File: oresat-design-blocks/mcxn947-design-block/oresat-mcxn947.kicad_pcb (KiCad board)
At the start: 4 copper layers, 153 x 110 mm, 68 parts, among them J1 BKUP-BATT, J2 USB_C_Receptacle_USB2.0_14P, J3 CAN, J4 TERM, J5 10pin ARM SWD, J6 FTDI-UART-6PIN, SW1 RESET, SW2 ISP(BOOT), U1 MCXN947VKLT, U2 TCAN330, Y1 24 MHz, Y2 32.768 KHz

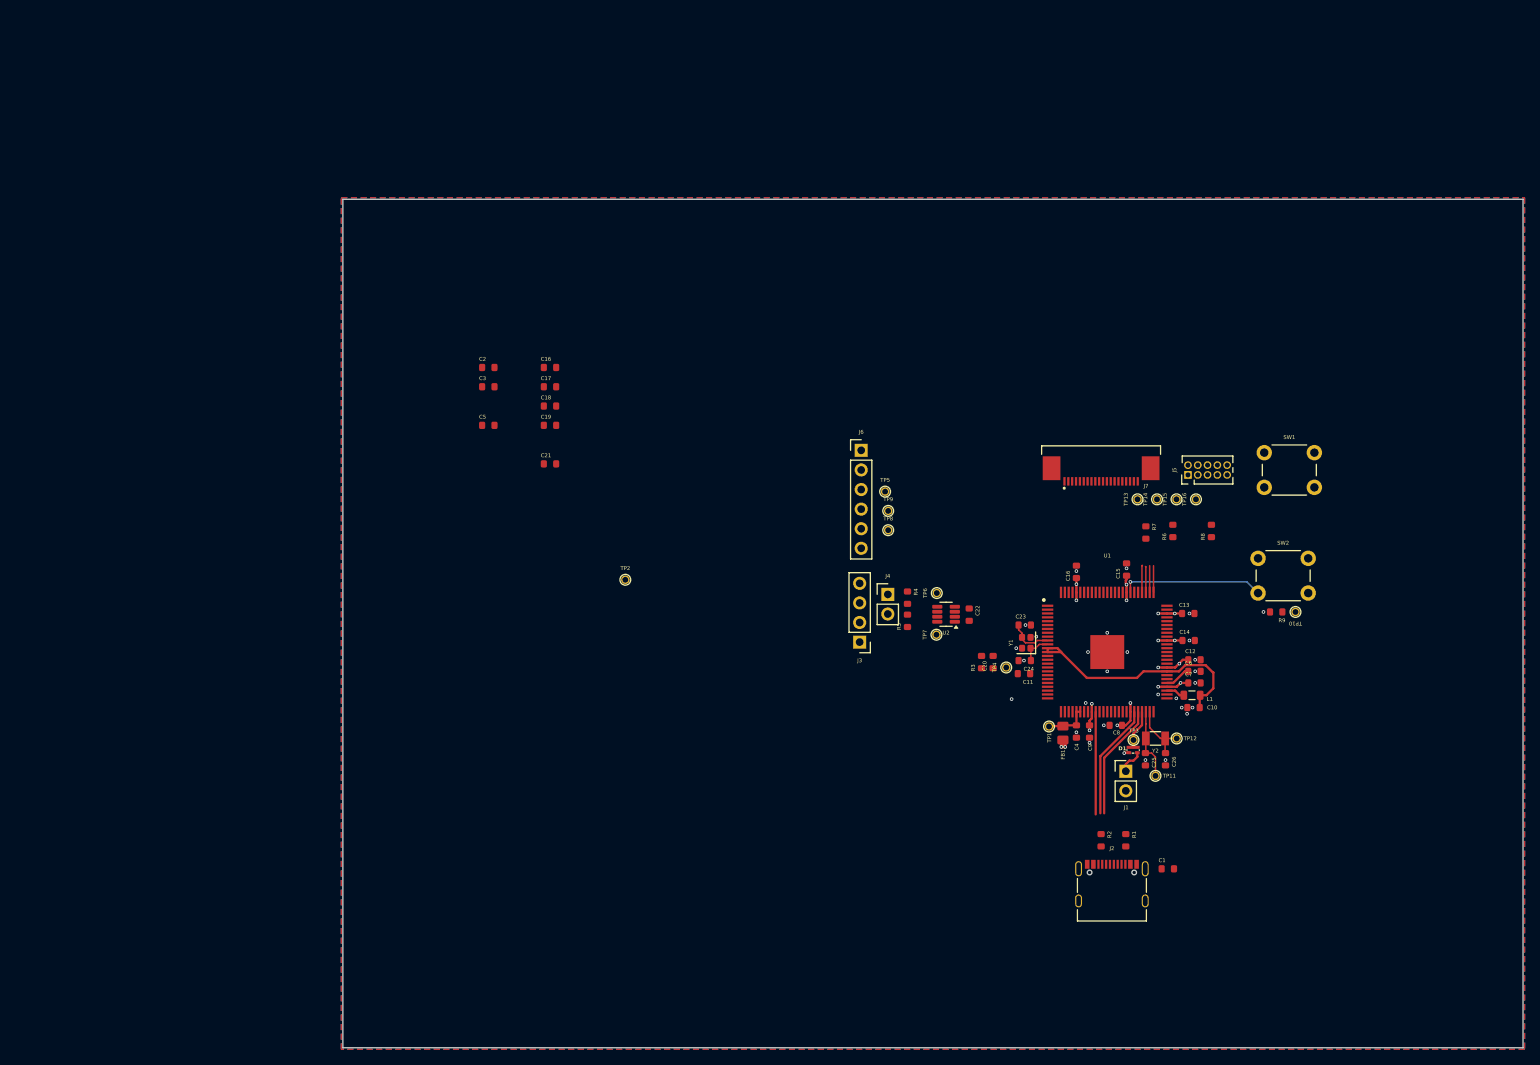
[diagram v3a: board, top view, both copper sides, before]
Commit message: Added 3.3V SPS but not hooked up yet. Everything else a rough draft, except for pin breakouts.
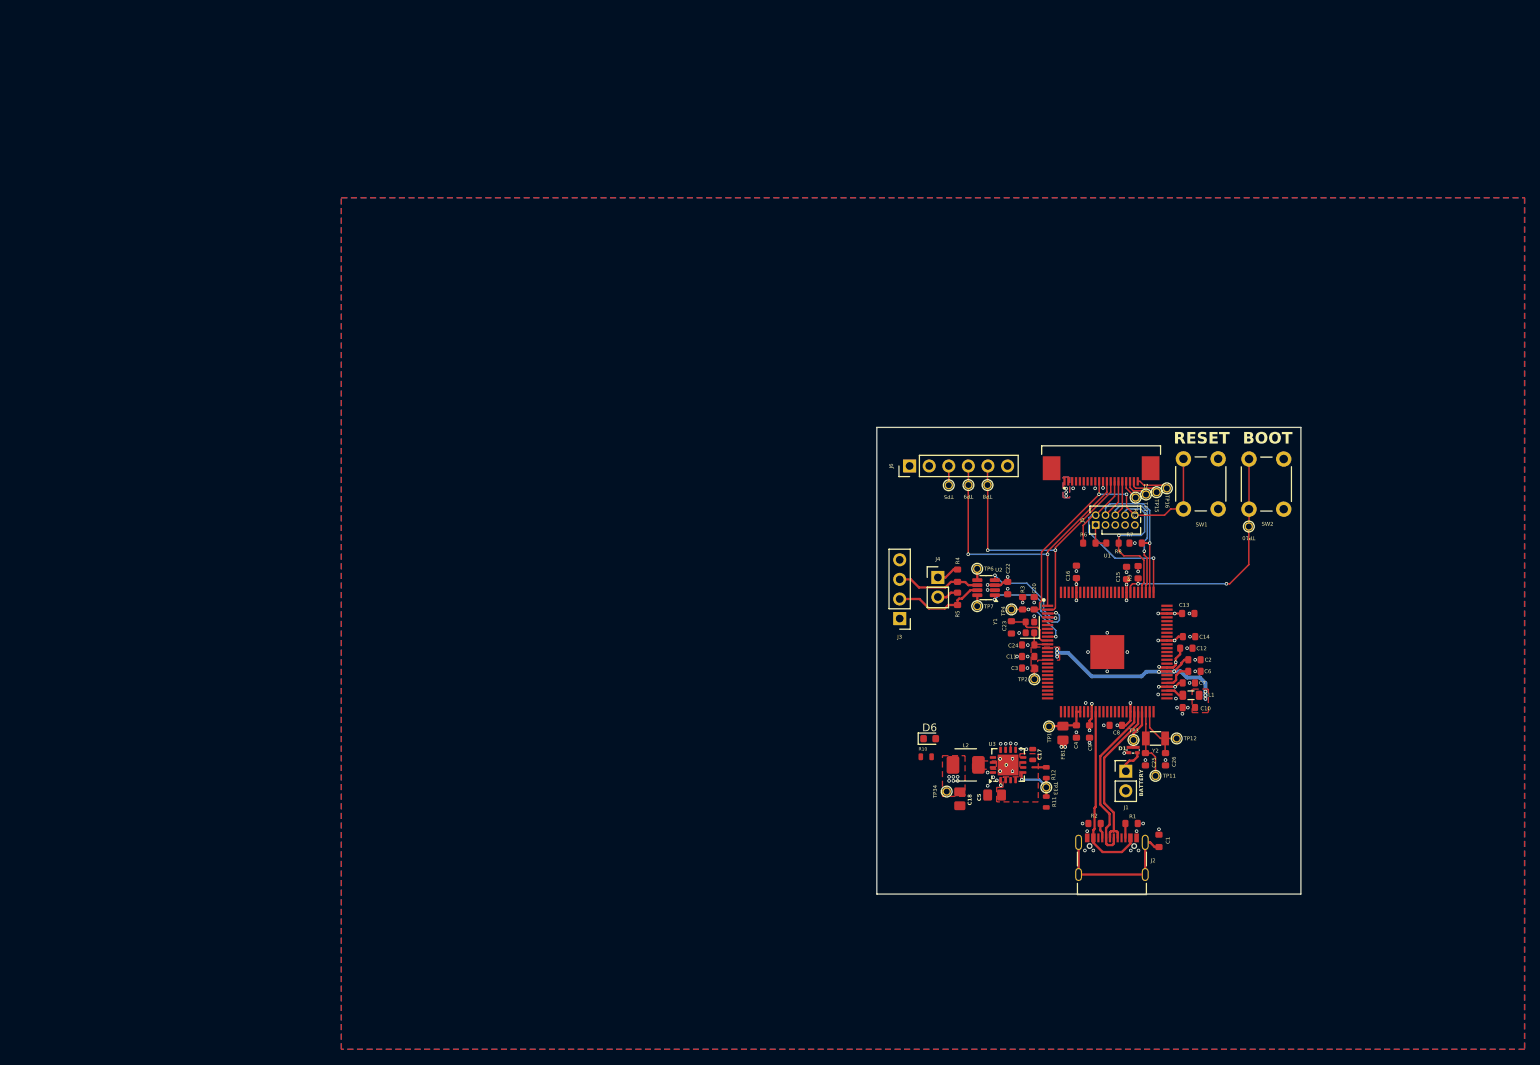
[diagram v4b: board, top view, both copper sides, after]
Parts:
- removed the C16 at (88.3, 63.8)
- removed C19, C21: 100n, oresat-passives:0603-B-NOSILK
- added D6: GREEN, LED_SMD:LED_0603_1608Metric, F.Cu at (137.5, 111.9)
- added L2: 6.8u, oresat-passives:L_ECS-MPI4040, F.Cu at (142.1, 115.3)
- added R10: 10k, oresat-passives:0603-C-NOSILK, F.Cu at (137.0, 114.3)
- added R11: 10k, oresat-passives:0603-C-NOSILK, F.Cu at (152.6, 120.1)
- added R12: 10k, oresat-passives:0603-C-NOSILK, F.Cu at (152.6, 116.3)
- added TP33: Test-Point, oresat-misc:TestPoint-0.75mm-th, F.Cu at (152.6, 118.2)
- added TP34: Test-Point, oresat-misc:TestPoint-0.75mm-th, F.Cu at (139.7, 118.8)
- added U3: TPS62111RSA, Package_DFN_QFN:Texas_RSA_VQFN-16-1EP_4x4mm_P0.65mm_EP2.7x2.7mm, F.Cu at (147.6, 115.3)
- C17: value 100n -> 1u; footprint oresat-passives:0603-B-NOSILK -> oresat-passives:0603-C-NOSILK
- C18: value 100n -> 22u; footprint oresat-passives:0603-B-NOSILK -> oresat-passives:0805-B-NOSILK
- C5: value 100n -> 10u; footprint oresat-passives:0603-B-NOSILK -> oresat-passives:0805-B-NOSILK
- moved C2 99.1 mm to (171.8, 101.7)
- moved C5 81.3 mm to (145.9, 119.2), turned to 180 degrees
- moved C3 78.9 mm to (150.2, 102.8), turned to 180 degrees
- moved C17 78.7 mm to (150.8, 114.0), turned to 90 degrees
- moved C18 73.6 mm to (141.4, 119.7), turned to -90 degrees
- moved TP2 54.6 mm to (151.1, 104.2)
- moved R9 18.6 mm to (164.5, 90.3), turned to 90 degrees
- moved TP8 14.1 mm to (145.0, 79.0), turned to 180 degrees
- moved J5 13.6 mm to (159.0, 84.2)
- moved SW2 13.3 mm to (183.4, 75.7), turned to -90 degrees
- moved R8 12.9 mm to (161.2, 86.6), turned to 180 degrees
- moved SW1 12.8 mm to (170.4, 82.2), turned to 90 degrees
- moved TP10 12.6 mm to (178.8, 84.4)
- moved R6 10.9 mm to (158.2, 86.6), turned to 0 degrees
- moved TP9 10.9 mm to (142.5, 79.0), turned to 180 degrees
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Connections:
- C17 pad 1: +3.3V -> VBUS
- C5 pad 1: VDD -> VBUS
- J3 pad 1: +3.3V -> VBUS
- J7 pad 1: +3.3V -> VBUS
- J7 pad 2: +3.3V -> VBUS
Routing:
- net VBUS: track 13.3 -> 101.2 mm, vias 0 -> 3
- net RESET: track 0.00 -> 49.8 mm, vias 0 -> 4
- net /ISP-UART_RXD: track 0.00 -> 41.1 mm, vias 0 -> 2
- net /ISP-UART_TXD: track 0.00 -> 40.2 mm, vias 0 -> 2
- net /SWDIO: track 3.46 -> 27.0 mm, vias 0 -> 1
- net /SWCLK: track 3.46 -> 24.6 mm, vias 0 -> 1
- net Net-(J2-SHIELD): track 0.00 -> 19.0 mm
- net /SWO: track 3.38 -> 20.9 mm, vias 0 -> 1
- net /SWI: track 3.53 -> 19.4 mm, vias 0 -> 1
- net /CAN_TXD: track 0.00 -> 13.8 mm, vias 0 -> 2
- net /BOOT: track 18.5 -> 31.7 mm, vias 1 -> 2
- net /CAN_RXD: track 0.00 -> 12.6 mm, vias 0 -> 2
- net /CANH: track 0.00 -> 11.9 mm
- net /CANL: track 0.00 -> 11.0 mm
- net +3.3V: track 32.8 -> 42.5 mm, vias 20 -> 31
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- added copper zone on F.Cu, net +3.3V
- added copper zone on In2.Cu, net GND
- added copper zone on F.Cu, net Net-(L2-Pad1)
- added copper zone on B.Cu, net VBUS
- added copper zone on F.Cu, net VBUS
- added copper zone on In2.Cu, net VBUS
- added copper zone on F.Cu, net VDD
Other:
- board size 153 x 110 mm -> 55 x 60.5 mm
- board text added: "BATTERY"
- board text added: "BOOT"
- board text added: "RESET"

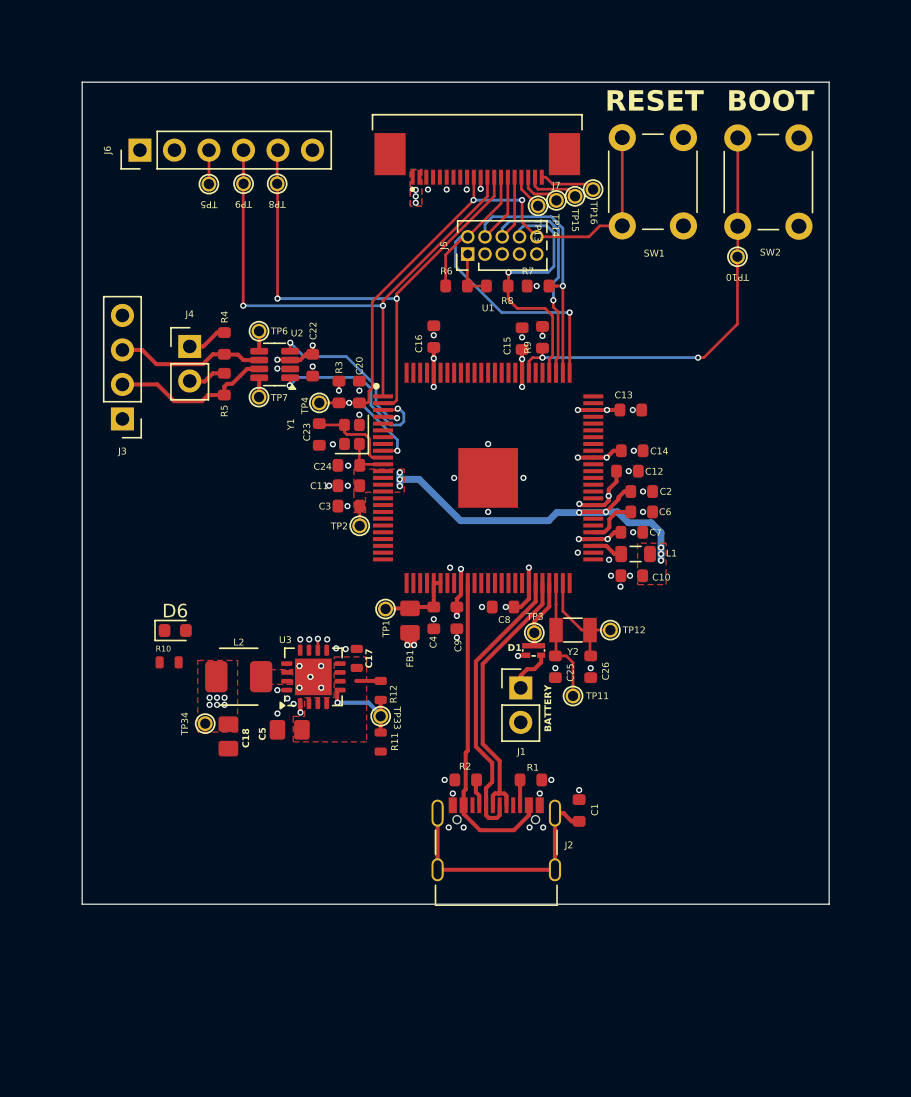
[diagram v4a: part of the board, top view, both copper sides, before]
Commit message: added hierarchal sheets, cleaned up schematic, added and routed breakout connectors
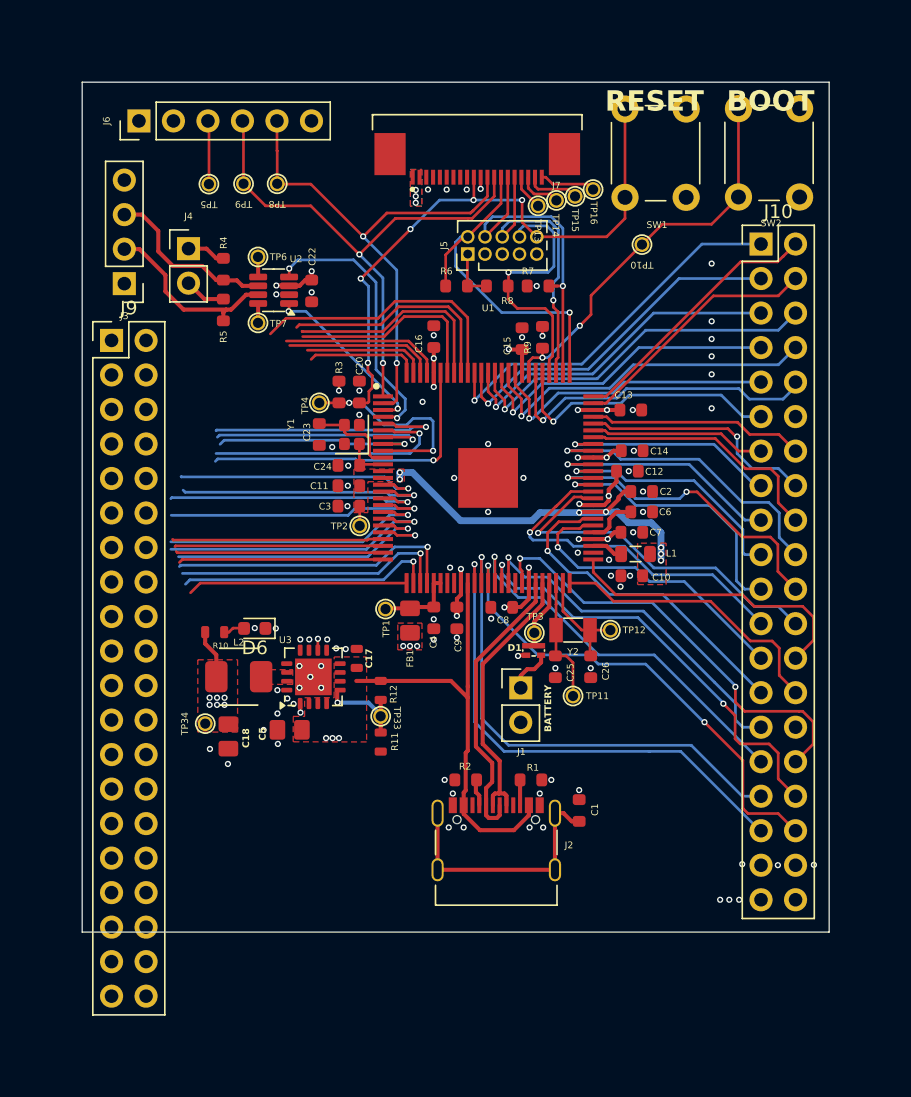
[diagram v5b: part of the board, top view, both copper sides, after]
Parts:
- added J10: Conn_02x20_Odd_Even, Connector_PinHeader_2.54mm:PinHeader_2x20_P2.54mm_Vertical, F.Cu at (180.6, 83.5)
- added J9: Conn_02x20_Odd_Even, Connector_PinHeader_2.54mm:PinHeader_2x20_P2.54mm_Vertical, F.Cu at (132.8, 90.6)
- moved J3 9.96 mm to (133.7, 86.4)
- moved J4 7.20 mm to (138.4, 83.8)
- moved TP10 7.08 mm to (171.8, 83.5)
- moved D6 5.86 mm to (143.3, 111.8), turned to 180 degrees
- moved C22 5.46 mm to (147.5, 86.9)
- moved TP6 5.46 mm to (143.6, 84.4)
- moved TP7 5.46 mm to (143.6, 89.3)
- moved R4 5.46 mm to (141.0, 85.3)
- moved R5 5.46 mm to (141.0, 88.3)
- moved U2 5.46 mm to (144.7, 86.9)
- moved R10 4.02 mm to (140.4, 112.0), turned to 180 degrees
- moved J6 2.15 mm to (134.8, 74.4)
- moved SW2 2.15 mm to (183.4, 73.5)
- moved SW1 2.11 mm to (170.6, 80.0)
- moved C8 0.10 mm to (161.5, 110.2)
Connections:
- net /BOOT renamed /Power & Signal/BOOT
- net /CANH renamed /Power & Signal/CANH
- net /CANL renamed /Power & Signal/CANL
- net /CAN_RXD renamed Net-(U1C-P1_11)
- net /CAN_TXD renamed Net-(U1C-P1_10)
- net /SWI renamed Net-(J5-NC/TDI)
- J5 pad 2: /SWDIO -> Net-(J5-SWDIO/TMS)
- J5 pad 4: /SWCLK -> Net-(J5-SWCLK/TCK)
- J5 pad 6: /SWO -> Net-(J5-SWO/TDO)
- J6 pad 4: /ISP-UART_RXD -> Net-(J6-TXD)
- J6 pad 5: /ISP-UART_TXD -> Net-(J6-RXD)
- J7 pad 12: /ISP-UART_RXD -> ISP-UART_RXD
- J7 pad 13: /ISP-UART_TXD -> ISP-UART_TXD
- J7 pad 14: /SWDIO -> SWDIO
- J7 pad 15: /SWCLK -> SWCLK
- J7 pad 16: /SWO -> SWO
- R6 pad 1: /SWDIO -> Net-(J5-SWDIO/TMS)
- R7 pad 2: /SWCLK -> Net-(J5-SWCLK/TCK)
- TP8 pad 1: /ISP-UART_TXD -> Net-(J6-RXD)
- TP9 pad 1: /ISP-UART_RXD -> Net-(J6-TXD)
- U1 pad 1: /ISP-UART_RXD -> Net-(J6-TXD)
- U1 pad 100: unconnected-(U1C-P1_7-Pad100) -> P1_7
- U1 pad 2: /ISP-UART_TXD -> Net-(J6-RXD)
- U1 pad 36: unconnected-(U1F-P4_13/ANA_14-Pad36) -> P4_13
- U1 pad 37: unconnected-(U1F-P4_15-Pad37) -> P4_15
- U1 pad 38: unconnected-(U1F-P4_16-Pad38) -> P4_16
- U1 pad 39: unconnected-(U1F-P4_17/ANA_18-Pad39) -> P4_17
- U1 pad 40: unconnected-(U1F-P4_19-Pad40) -> P4_19
- U1 pad 41: unconnected-(U1F-P4_20-Pad41) -> P4_20
- U1 pad 43: unconnected-(U1F-P4_23-Pad43) -> P4_23
- U1 pad 5: unconnected-(U1C-P1_12-Pad5) -> P1_12
- U1 pad 50: unconnected-(U1G-P5_2-Pad50) -> P5_2
- U1 pad 51: unconnected-(U1G-P5_3-Pad51) -> P5_3
- U1 pad 56: unconnected-(U1E-P3_21-Pad56) -> Net-(J10-Pin_25)
- U1 pad 57: unconnected-(U1E-P3_20-Pad57) -> Net-(J10-Pin_27)
- U1 pad 6: unconnected-(U1C-P1_13-Pad6) -> P1_13
- U1 pad 60: unconnected-(U1E-P3_17-Pad60) -> Net-(J10-Pin_24)
- U1 pad 61: unconnected-(U1E-P3_16-Pad61) -> Net-(J10-Pin_23)
- U1 pad 62: unconnected-(U1E-P3_15-Pad62) -> Net-(J10-Pin_21)
- U1 pad 63: unconnected-(U1E-P3_14-Pad63) -> Net-(J10-Pin_22)
- U1 pad 64: unconnected-(U1E-P3_13-Pad64) -> Net-(J10-Pin_19)
- U1 pad 65: unconnected-(U1E-P3_12-Pad65) -> Net-(J10-Pin_17)
- U1 pad 67: unconnected-(U1E-P3_11-Pad67) -> Net-(J10-Pin_20)
- U1 pad 68: unconnected-(U1E-P3_10-Pad68) -> Net-(J10-Pin_15)
- U1 pad 69: unconnected-(U1E-P3_9-Pad69) -> Net-(J10-Pin_18)
- U1 pad 7: unconnected-(U1C-P1_14-Pad7) -> P1_14
- U1 pad 70: unconnected-(U1E-P3_8-Pad70) -> Net-(J10-Pin_13)
- U1 pad 71: unconnected-(U1E-P3_7-Pad71) -> Net-(J10-Pin_16)
- U1 pad 72: unconnected-(U1E-P3_6-Pad72) -> Net-(J10-Pin_14)
- U1 pad 74: unconnected-(U1E-P3_1-Pad74) -> Net-(J10-Pin_4)
- U1 pad 75: unconnected-(U1E-P3_0-Pad75) -> Net-(J10-Pin_2)
- U1 pad 76: /SWDIO -> Net-(J5-SWDIO/TMS)
- U1 pad 77: /SWCLK -> Net-(J5-SWCLK/TCK)
- U1 pad 78: /SWO -> Net-(J5-SWO/TDO)
- U1 pad 8: unconnected-(U1C-P1_15-Pad8) -> P1_15
- U1 pad 80: unconnected-(U1B-P0_4-Pad80) -> P0_4
- U1 pad 81: unconnected-(U1B-P0_5-Pad81) -> P0_5
- U1 pad 84: unconnected-(U1B-P0_16-Pad84) -> P0_16
- U1 pad 85: unconnected-(U1B-P0_17-Pad85) -> P0_17
- U1 pad 86: unconnected-(U1B-P0_18-Pad86) -> P0_18
- U1 pad 87: unconnected-(U1B-P0_19-Pad87) -> P0_19
- U1 pad 88: unconnected-(U1B-P0_20-Pad88) -> P0_20
- U1 pad 89: unconnected-(U1B-P0_21-Pad89) -> P0_21
- U1 pad 90: unconnected-(U1B-P0_22-Pad90) -> P0_22
- U1 pad 91: unconnected-(U1B-P0_23-Pad91) -> P0_23
- U1 pad 92: unconnected-(U1C-P1_0-Pad92) -> P1_0
- U1 pad 93: unconnected-(U1C-P1_1-Pad93) -> P1_1
- U1 pad 94: unconnected-(U1C-P1_2-Pad94) -> P1_2
- U1 pad 95: unconnected-(U1C-P1_3-Pad95) -> P1_3
- U1 pad 97: unconnected-(U1C-P1_4-Pad97) -> P1_4
- U1 pad 98: unconnected-(U1C-P1_5-Pad98) -> P1_5
- U1 pad 99: unconnected-(U1C-P1_6-Pad99) -> P1_6
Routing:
- net /ISP-UART_RXD: track 41.1 -> 0.00 mm, vias 2 -> 0
- net /ISP-UART_TXD: track 40.2 -> 0.00 mm, vias 2 -> 0
- net P4_13: track 0.00 -> 37.6 mm, vias 0 -> 1
- net P4_15: track 0.00 -> 36.7 mm, vias 0 -> 1
- net P4_16: track 0.00 -> 35.8 mm, vias 0 -> 2
- net Net-(J6-RXD): track 0.00 -> 35.6 mm, vias 0 -> 2
- net P4_23: track 0.00 -> 32.6 mm, vias 0 -> 2
- net P4_19: track 0.00 -> 32.5 mm, vias 0 -> 2
- net P4_17: track 0.00 -> 28.7 mm, vias 0 -> 1
- net P0_22: track 0.00 -> 27.9 mm, vias 0 -> 1
- net P0_19: track 0.00 -> 27.3 mm, vias 0 -> 1
- net Net-(J10-Pin_24): track 0.00 -> 27.0 mm, vias 0 -> 1
- net SWDIO: track 0.00 -> 27.0 mm, vias 0 -> 1
- net /SWDIO: track 27.0 -> 0.00 mm, vias 1 -> 0
- net P4_20: track 0.00 -> 26.5 mm, vias 0 -> 1
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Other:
- board size 55 x 60.5 mm -> 55 x 62.5 mm
